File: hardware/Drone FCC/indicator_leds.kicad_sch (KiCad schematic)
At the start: 50 parts, among them Q1101 2N7002, Q1102 2N7002, Q1103 2N7002, Q1104 2N7002, Q1105 2N7002, Q1106 2N7002, Q1107 2N7002, Q1108 2N7002, SW1101 SW Proposito General, SW1102 SW Proposito General

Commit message: set values of resistors for LEDs
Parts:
- R1101, R1104, R1107, R1110, R1113, R1116, R1119, R1122: value R -> 100k
- R1102, R1105, R1108, R1111, R1114, R1117, R1120, R1123: value R -> 33k
- R1103, R1106, R1109, R1112, R1115, R1118, R1121, R1124: value R -> 220
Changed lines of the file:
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@@
   (junction (at 118.11 17.145) (diameter 0) (color 0 0 0 0)
   )
-  (junction (at 46.355 167.64) (diameter 0) (color 0 0 0 0)
-  )
   (junction (at 119.38 182.245) (diameter 0) (color 0 0 0 0)
   )
@@
     (stroke (width 0) (type default) (color 0 0 0 0))
   )
-  (wire (pts (xy 46.355 167.64) (xy 46.355 167.005))
-    (stroke (width 0) (type default) (color 0 0 0 0))
-  )
   (wire (pts (xy 118.11 29.845) (xy 118.11 32.385))
     (stroke (width 0) (type default) (color 0 0 0 0))
@@
     (stroke (width 0) (type default) (color 0 0 0 0))
   )
-  (wire (pts (xy 42.545 167.64) (xy 46.355 167.64))
-    (stroke (width 0) (type default) (color 0 0 0 0))
-  )
   (wire (pts (xy 40.005 167.64) (xy 42.545 167.64))
     (stroke (width 0) (type default) (color 0 0 0 0))
@@
     (stroke (width 0) (type default) (color 0 0 0 0))
   )
-  (wire (pts (xy 46.355 167.64) (xy 51.435 167.64))
+  (wire (pts (xy 42.545 167.64) (xy 51.435 167.64))
     (stroke (width 0) (type default) (color 0 0 0 0))
   )
@@
     (in_bom yes) (on_board yes) (fields_autoplaced)
     (property "Reference" "R1102" (id 0) (at 55.88 41.91 90))
-    (property "Value" "R" (id 1) (at 55.88 44.45 90))
+    (property "Value" "33k" (id 1) (at 55.88 44.45 90))
     (property "Footprint" "Resistor_SMD:R_0402_1005Metric_Pad0.72x0.64mm_HandSolder" (id 2) (at 55.88 49.403 90)
       (effects (font (size 1.27 1.27)) hide)
@@
   (symbol (lib_id "Device:R") (at 95.885 133.985 180) (unit 1)
     (in_bom yes) (on_board yes) (fields_autoplaced)
-    (property "Reference" "R1116" (id 0) (at 98.425 132.7149 0)
-      (effects (font (size 1.27 1.27)) (justify right))
-    )
-    (property "Value" "R" (id 1) (at 98.425 135.2549 0)
+    (property "Reference" "R1116" (id 0) (at 97.79 132.7149 0)
+      (effects (font (size 1.27 1.27)) (justify right))
+    )
+    (property "Value" "100k" (id 1) (at 97.79 135.2549 0)
       (effects (font (size 1.27 1.27)) (justify right))
     )
@@
   (symbol (lib_id "Device:R") (at 47.625 133.985 180) (unit 1)
     (in_bom yes) (on_board yes) (fields_autoplaced)
-    (property "Reference" "R1113" (id 0) (at 50.165 132.7149 0)
-      (effects (font (size 1.27 1.27)) (justify right))
-    )
-    (property "Value" "R" (id 1) (at 50.165 135.2549 0)
+    (property "Reference" "R1113" (id 0) (at 49.53 132.7149 0)
+      (effects (font (size 1.27 1.27)) (justify right))
+    )
+    (property "Value" "100k" (id 1) (at 49.53 135.2549 0)
       (effects (font (size 1.27 1.27)) (justify right))
     )
@@
       (effects (font (size 1.27 1.27)) (justify right))
     )
-    (property "Value" "R" (id 1) (at 175.26 135.2549 0)
+    (property "Value" "100k" (id 1) (at 175.26 135.2549 0)
       (effects (font (size 1.27 1.27)) (justify right))
     )
@@
   (symbol (lib_id "Device:R") (at 67.945 116.205 180) (unit 1)
     (in_bom yes) (on_board yes) (fields_autoplaced)
-    (property "Reference" "R1115" (id 0) (at 70.485 114.9349 0)
-      (effects (font (size 1.27 1.27)) (justify right))
-    )
-    (property "Value" "R" (id 1) (at 70.485 117.4749 0)
+    (property "Reference" "R1115" (id 0) (at 69.85 114.9349 0)
+      (effects (font (size 1.27 1.27)) (justify right))
+    )
+    (property "Value" "220" (id 1) (at 69.85 117.4749 0)
       (effects (font (size 1.27 1.27)) (justify right))
     )
@@
       (effects (font (size 1.27 1.27)) (justify right))
     )
-    (property "Value" "R" (id 1) (at 243.84 37.4649 0)
+    (property "Value" "220" (id 1) (at 243.84 37.4649 0)
       (effects (font (size 1.27 1.27)) (justify right))
     )
@@
       (effects (font (size 1.27 1.27)) (justify right))
     )
-    (property "Value" "R" (id 1) (at 223.52 55.2449 0)
+    (property "Value" "100k" (id 1) (at 223.52 55.2449 0)
       (effects (font (size 1.27 1.27)) (justify right))
     )
@@
       (effects (font (size 1.27 1.27)) (justify right))
     )
-    (property "Value" "R" (id 1) (at 120.65 37.4649 0)
+    (property "Value" "220" (id 1) (at 120.65 37.4649 0)
       (effects (font (size 1.27 1.27)) (justify right))
     )
@@
     (in_bom yes) (on_board yes) (fields_autoplaced)
     (property "Reference" "R1108" (id 0) (at 179.07 41.91 90))
-    (property "Value" "R" (id 1) (at 179.07 44.45 90))
+    (property "Value" "33k" (id 1) (at 179.07 44.45 90))
     (property "Footprint" "Resistor_SMD:R_0402_1005Metric_Pad0.72x0.64mm_HandSolder" (id 2) (at 179.07 49.403 90)
       (effects (font (size 1.27 1.27)) hide)
@@
     (in_bom yes) (on_board yes) (fields_autoplaced)
     (property "Reference" "R1114" (id 0) (at 53.975 121.92 90))
-    (property "Value" "R" (id 1) (at 53.975 124.46 90))
+    (property "Value" "33k" (id 1) (at 53.975 124.46 90))
     (property "Footprint" "Resistor_SMD:R_0402_1005Metric_Pad0.72x0.64mm_HandSolder" (id 2) (at 53.975 129.413 90)
       (effects (font (size 1.27 1.27)) hide)
@@
       (effects (font (size 1.27 1.27)) (justify right))
     )
-    (property "Value" "R" (id 1) (at 72.39 37.4649 0)
+    (property "Value" "220" (id 1) (at 72.39 37.4649 0)
       (effects (font (size 1.27 1.27)) (justify right))
     )
@@
       (effects (font (size 1.27 1.27)) (justify right))
     )
-    (property "Value" "R" (id 1) (at 52.07 55.2449 0)
+    (property "Value" "100k" (id 1) (at 52.07 55.2449 0)
       (effects (font (size 1.27 1.27)) (justify right))
     )
@@
       (effects (font (size 1.27 1.27)) (justify right))
     )
-    (property "Value" "R" (id 1) (at 223.52 135.2549 0)
+    (property "Value" "100k" (id 1) (at 223.52 135.2549 0)
       (effects (font (size 1.27 1.27)) (justify right))
     )
@@
     (in_bom yes) (on_board yes) (fields_autoplaced)
     (property "Reference" "R1123" (id 0) (at 227.33 121.92 90))
-    (property "Value" "R" (id 1) (at 227.33 124.46 90))
+    (property "Value" "33k" (id 1) (at 227.33 124.46 90))
     (property "Footprint" "Resistor_SMD:R_0402_1005Metric_Pad0.72x0.64mm_HandSolder" (id 2) (at 227.33 129.413 90)
       (effects (font (size 1.27 1.27)) hide)
@@
       (effects (font (size 1.27 1.27)) (justify right))
     )
-    (property "Value" "R" (id 1) (at 100.33 55.2449 0)
+    (property "Value" "100k" (id 1) (at 100.33 55.2449 0)
       (effects (font (size 1.27 1.27)) (justify right))
     )
@@
       (effects (font (size 1.27 1.27)) (justify right))
     )
-    (property "Value" "R" (id 1) (at 195.58 117.4749 0)
+    (property "Value" "220" (id 1) (at 195.58 117.4749 0)
       (effects (font (size 1.27 1.27)) (justify right))
     )
@@
       (effects (font (size 1.27 1.27)) (justify right))
     )
-    (property "Value" "R" (id 1) (at 175.26 55.2449 0)
+    (property "Value" "100k" (id 1) (at 175.26 55.2449 0)
       (effects (font (size 1.27 1.27)) (justify right))
     )
@@
     (in_bom yes) (on_board yes) (fields_autoplaced)
     (property "Reference" "R1120" (id 0) (at 179.07 121.92 90))
-    (property "Value" "R" (id 1) (at 179.07 124.46 90))
+    (property "Value" "33k" (id 1) (at 179.07 124.46 90))
     (property "Footprint" "Resistor_SMD:R_0402_1005Metric_Pad0.72x0.64mm_HandSolder" (id 2) (at 179.07 129.413 90)
       (effects (font (size 1.27 1.27)) hide)
@@
     (in_bom yes) (on_board yes) (fields_autoplaced)
     (property "Reference" "R1105" (id 0) (at 104.14 41.91 90))
-    (property "Value" "R" (id 1) (at 104.14 44.45 90))
+    (property "Value" "33k" (id 1) (at 104.14 44.45 90))
     (property "Footprint" "Resistor_SMD:R_0402_1005Metric_Pad0.72x0.64mm_HandSolder" (id 2) (at 104.14 49.403 90)
       (effects (font (size 1.27 1.27)) hide)
@@
       (effects (font (size 1.27 1.27)) (justify right))
     )
-    (property "Value" "R" (id 1) (at 243.84 117.4749 0)
+    (property "Value" "220" (id 1) (at 243.84 117.4749 0)
       (effects (font (size 1.27 1.27)) (justify right))
     )
@@
     (in_bom yes) (on_board yes) (fields_autoplaced)
     (property "Reference" "R1117" (id 0) (at 102.235 121.92 90))
-    (property "Value" "R" (id 1) (at 102.235 124.46 90))
+    (property "Value" "33k" (id 1) (at 102.235 124.46 90))
     (property "Footprint" "Resistor_SMD:R_0402_1005Metric_Pad0.72x0.64mm_HandSolder" (id 2) (at 102.235 129.413 90)
       (effects (font (size 1.27 1.27)) hide)
@@
       (effects (font (size 1.27 1.27)) (justify right))
     )
-    (property "Value" "R" (id 1) (at 195.58 37.4649 0)
+    (property "Value" "220" (id 1) (at 195.58 37.4649 0)
       (effects (font (size 1.27 1.27)) (justify right))
     )
@@
     (in_bom yes) (on_board yes) (fields_autoplaced)
     (property "Reference" "R1111" (id 0) (at 227.33 41.91 90))
-    (property "Value" "R" (id 1) (at 227.33 44.45 90))
+    (property "Value" "33k" (id 1) (at 227.33 44.45 90))
     (property "Footprint" "Resistor_SMD:R_0402_1005Metric_Pad0.72x0.64mm_HandSolder" (id 2) (at 227.33 49.403 90)
       (effects (font (size 1.27 1.27)) hide)
@@
   (symbol (lib_id "Device:R") (at 116.205 116.205 180) (unit 1)
     (in_bom yes) (on_board yes) (fields_autoplaced)
-    (property "Reference" "R1118" (id 0) (at 118.745 114.9349 0)
-      (effects (font (size 1.27 1.27)) (justify right))
-    )
-    (property "Value" "R" (id 1) (at 118.745 117.4749 0)
-      (effects (font (size 1.27 1.27)) (justify right))
-    )
+    (property "Reference" "R1118" (id 0) (at 118.11 114.9349 0)
+      (effects (font (size 1.27 1.27)) (justify right))
+    )
+    (property "Value" "220" (id 1) (at 118.11 117.4749 0)
+      (effects (font (size 1.27 1.27)) (justify right))
+    )

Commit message: moved some LEDs over the oppsoite layer of microSD footprint
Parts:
- R1103, R1106, R1109, R1112, R1115, R1118, R1121, R1124: footprint Resistor_SMD:R_0805_2012Metric_Pad1.20x1.40mm_HandSolder -> Resistor_SMD:R_0402_1005Metric_Pad0.72x0.64mm_HandSolder

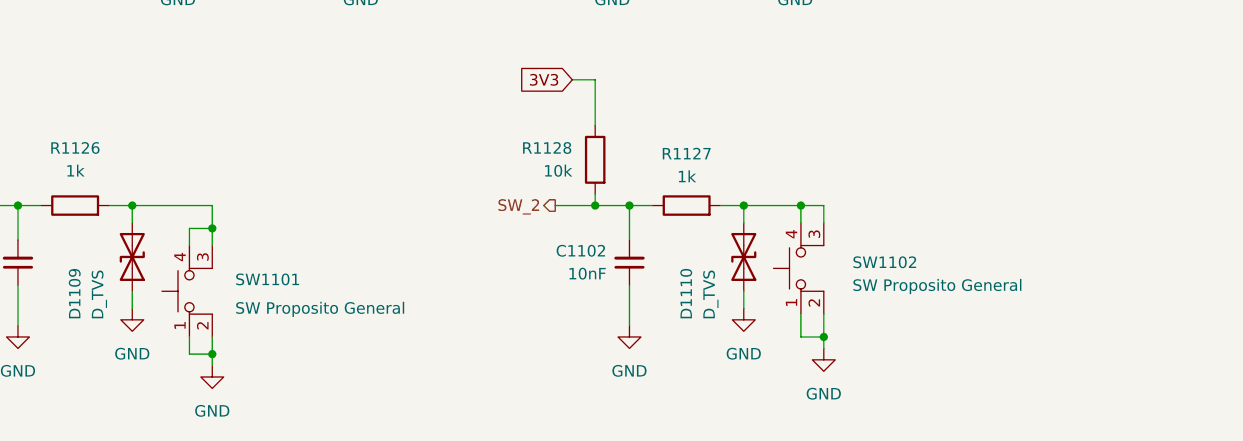
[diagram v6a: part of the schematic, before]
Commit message: changed sw with smaller sw
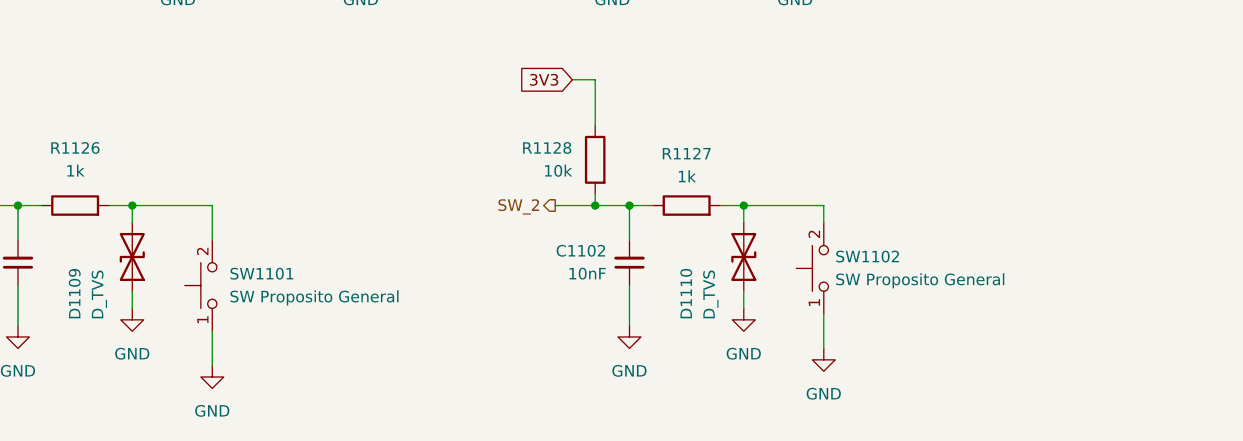
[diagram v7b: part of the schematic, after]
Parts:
- removed SW1101, SW1102: SW Proposito General, TL3305AF160QG:SW_TL3305AF160QG, symbol Switch:SW_MEC_5E
- added SW1101, SW1102: SW Proposito General, 434121043816:434121043816, symbol 434121043816:SW_SPST
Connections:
- net GND: now also SW1101.1 (A), SW1102.1 (A)
- net at D1110.2 (A2), R1127.2: now also SW1102.2 (B)
- net at D1109.2 (A2), R1126.2: now also SW1101.2 (B)
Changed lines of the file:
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@@
   (junction (at 118.11 17.145) (diameter 0) (color 0 0 0 0)
   )
-  (junction (at 119.38 182.245) (diameter 0) (color 0 0 0 0)
-  )
-  (junction (at 51.435 170.18) (diameter 0) (color 0 0 0 0)
-  )
   (junction (at 29.845 167.64) (diameter 0) (color 0 0 0 0)
   )
@@
   (junction (at 67.945 97.155) (diameter 0) (color 0 0 0 0)
   )
-  (junction (at 51.435 184.15) (diameter 0) (color 0 0 0 0)
-  )
   (junction (at 26.035 167.64) (diameter 0) (color 0 0 0 0)
   )
@@
   (junction (at 116.205 97.155) (diameter 0) (color 0 0 0 0)
   )
-  (junction (at 116.84 167.64) (diameter 0) (color 0 0 0 0)
-  )
   (junction (at 193.04 97.155) (diameter 0) (color 0 0 0 0)
   )
@@
     (stroke (width 0) (type default) (color 0 0 0 0))
   )
-  (wire (pts (xy 116.84 167.64) (xy 116.84 169.545))
+  (wire (pts (xy 51.435 167.64) (xy 51.435 171.45))
     (stroke (width 0) (type default) (color 0 0 0 0))
   )
@@
     (stroke (width 0) (type default) (color 0 0 0 0))
   )
-  (wire (pts (xy 51.435 184.15) (xy 51.435 185.42))
-    (stroke (width 0) (type default) (color 0 0 0 0))
-  )
   (wire (pts (xy 193.04 132.715) (xy 193.04 140.335))
     (stroke (width 0) (type default) (color 0 0 0 0))
@@
     (stroke (width 0) (type default) (color 0 0 0 0))
   )
-  (wire (pts (xy 116.84 167.64) (xy 119.38 167.64))
+  (wire (pts (xy 110.49 167.64) (xy 119.38 167.64))
     (stroke (width 0) (type default) (color 0 0 0 0))
   )
@@
     (stroke (width 0) (type default) (color 0 0 0 0))
   )
-  (wire (pts (xy 48.895 170.18) (xy 51.435 170.18))
-    (stroke (width 0) (type default) (color 0 0 0 0))
-  )
   (wire (pts (xy 89.535 167.64) (xy 93.98 167.64))
     (stroke (width 0) (type default) (color 0 0 0 0))
@@
     (stroke (width 0) (type default) (color 0 0 0 0))
   )
-  (wire (pts (xy 51.435 170.18) (xy 51.435 172.085))
-    (stroke (width 0) (type default) (color 0 0 0 0))
-  )
   (wire (pts (xy 57.785 127.635) (xy 60.325 127.635))
     (stroke (width 0) (type default) (color 0 0 0 0))
@@
     (stroke (width 0) (type default) (color 0 0 0 0))
   )
-  (wire (pts (xy 48.895 182.245) (xy 48.895 184.15))
-    (stroke (width 0) (type default) (color 0 0 0 0))
-  )
   (wire (pts (xy 40.005 167.64) (xy 42.545 167.64))
     (stroke (width 0) (type default) (color 0 0 0 0))
@@
     (stroke (width 0) (type default) (color 0 0 0 0))
   )
-  (wire (pts (xy 119.38 182.245) (xy 119.38 179.705))
+  (wire (pts (xy 119.38 179.705) (xy 119.38 183.515))
     (stroke (width 0) (type default) (color 0 0 0 0))
   )
@@
     (stroke (width 0) (type default) (color 0 0 0 0))
   )
-  (wire (pts (xy 48.895 172.085) (xy 48.895 170.18))
-    (stroke (width 0) (type default) (color 0 0 0 0))
-  )
   (wire (pts (xy 167.64 127.635) (xy 172.72 127.635))
     (stroke (width 0) (type default) (color 0 0 0 0))
@@
     (stroke (width 0) (type default) (color 0 0 0 0))
   )
-  (wire (pts (xy 116.84 179.705) (xy 116.84 182.245))
-    (stroke (width 0) (type default) (color 0 0 0 0))
-  )
   (wire (pts (xy 193.04 109.855) (xy 193.04 112.395))
     (stroke (width 0) (type default) (color 0 0 0 0))
@@
     (stroke (width 0) (type default) (color 0 0 0 0))
   )
-  (wire (pts (xy 119.38 182.245) (xy 119.38 183.515))
-    (stroke (width 0) (type default) (color 0 0 0 0))
-  )
   (wire (pts (xy 64.77 17.145) (xy 69.85 17.145))
     (stroke (width 0) (type default) (color 0 0 0 0))
   )
+  (wire (pts (xy 51.435 181.61) (xy 51.435 185.42))
+    (stroke (width 0) (type default) (color 0 0 0 0))
+  )
   (wire (pts (xy 172.72 127.635) (xy 172.72 130.175))
     (stroke (width 0) (type default) (color 0 0 0 0))
   )
-  (wire (pts (xy 48.895 184.15) (xy 51.435 184.15))
-    (stroke (width 0) (type default) (color 0 0 0 0))
-  )
   (wire (pts (xy 118.11 52.705) (xy 118.11 60.325))
     (stroke (width 0) (type default) (color 0 0 0 0))
@@
     (stroke (width 0) (type default) (color 0 0 0 0))
   )
-  (wire (pts (xy 110.49 167.64) (xy 116.84 167.64))
-    (stroke (width 0) (type default) (color 0 0 0 0))
-  )
   (wire (pts (xy 100.33 167.64) (xy 97.79 167.64))
     (stroke (width 0) (type default) (color 0 0 0 0))
   )
-  (wire (pts (xy 116.84 182.245) (xy 119.38 182.245))
-    (stroke (width 0) (type default) (color 0 0 0 0))
-  )
   (wire (pts (xy 116.205 109.855) (xy 116.205 112.395))
     (stroke (width 0) (type default) (color 0 0 0 0))
@@
     (stroke (width 0) (type default) (color 0 0 0 0))
   )
-  (wire (pts (xy 51.435 167.64) (xy 51.435 170.18))
-    (stroke (width 0) (type default) (color 0 0 0 0))
-  )
   (wire (pts (xy 110.49 167.64) (xy 110.49 169.545))
     (stroke (width 0) (type default) (color 0 0 0 0))
@@
   )
   (wire (pts (xy 50.165 127.635) (xy 47.625 127.635))
-    (stroke (width 0) (type default) (color 0 0 0 0))
-  )
-  (wire (pts (xy 51.435 182.245) (xy 51.435 184.15))
     (stroke (width 0) (type default) (color 0 0 0 0))
   )
@@
     (pin "2")
   )
-  (symbol (lib_id "Switch:SW_MEC_5E") (at 51.435 177.165 90) (unit 1)
-    (in_bom yes) (on_board yes)
-    (property "Reference" "SW1101" (id 0) (at 53.975 175.895 90)
-      (effects (font (size 1.27 1.27)) (justify right))
-    )
-    (property "Value" "SW Proposito General" (id 1) (at 53.975 179.07 90)
-      (effects (font (size 1.27 1.27)) (justify right))
-    )
-    (property "Footprint" "TL3305AF160QG:SW_TL3305AF160QG" (id 2) (at 43.815 177.165 0)
-      (effects (font (size 1.27 1.27)) hide)
-    )
-    (property "Datasheet" "http://www.apem.com/int/index.php?controller=attachment&id_attachment=1371" (id 3) (at 43.815 177.165 0)
-      (effects (font (size 1.27 1.27)) hide)
-    )
-    (pin "1")
-    (pin "2")
-    (pin "3")
-    (pin "4")
-  )
   (symbol (lib_id "Device:R") (at 220.98 53.975 180) (unit 1)
     (in_bom yes) (on_board yes) (fields_autoplaced)
@@
     (pin "2")
   )
+  (symbol (lib_id "434121043816:SW_SPST") (at 119.38 174.625 90) (unit 1)
+    (in_bom yes) (on_board yes)
+    (property "Reference" "SW1102" (id 0) (at 120.65 173.3549 90)
+      (effects (font (size 1.27 1.27)) (justify right))
+    )
+    (property "Value" "SW Proposito General" (id 1) (at 120.65 175.8949 90)
+      (effects (font (size 1.27 1.27)) (justify right))
+    )
+    (property "Footprint" "434121043816:434121043816" (id 2) (at 119.38 174.625 0)
+      (effects (font (size 1.27 1.27)) hide)
+    )
+    (property "Datasheet" "~" (id 3) (at 119.38 174.625 0)
+      (effects (font (size 1.27 1.27)) hide)
+    )
+    (pin "1")
+    (pin "2")
+  )
   (symbol (lib_id "Device:D_TVS") (at 42.545 173.355 270) (mirror x) (unit 1)
     (in_bom yes) (on_board yes)
@@
     (pin "1")
   )
+  (symbol (lib_id "434121043816:SW_SPST") (at 51.435 176.53 90) (unit 1)
+    (in_bom yes) (on_board yes) (fields_autoplaced)
+    (property "Reference" "SW1101" (id 0) (at 53.34 175.2599 90)
+      (effects (font (size 1.27 1.27)) (justify right))
+    )
+    (property "Value" "SW Proposito General" (id 1) (at 53.34 177.7999 90)
+      (effects (font (size 1.27 1.27)) (justify right))
+    )
+    (property "Footprint" "434121043816:434121043816" (id 2) (at 51.435 176.53 0)
+      (effects (font (size 1.27 1.27)) hide)
+    )
+    (property "Datasheet" "~" (id 3) (at 51.435 176.53 0)
+      (effects (font (size 1.27 1.27)) hide)
+    )
+    (pin "1")
+    (pin "2")
+  )
   (symbol (lib_id "Device:R") (at 97.79 53.975 180) (unit 1)
     (in_bom yes) (on_board yes) (fields_autoplaced)
@@
     (pin "1")
   )
-  (symbol (lib_id "Switch:SW_MEC_5E") (at 119.38 174.625 90) (unit 1)
-    (in_bom yes) (on_board yes)
-    (property "Reference" "SW1102" (id 0) (at 122.555 173.99 90)
-      (effects (font (size 1.27 1.27)) (justify right))
-    )
-    (property "Value" "SW Proposito General" (id 1) (at 122.555 176.53 90)
-      (effects (font (size 1.27 1.27)) (justify right))
-    )
-    (property "Footprint" "TL3305AF160QG:SW_TL3305AF160QG" (id 2) (at 111.76 174.625 0)
-      (effects (font (size 1.27 1.27)) hide)
-    )
-    (property "Datasheet" "http://www.apem.com/int/index.php?controller=attachment&id_attachment=1371" (id 3) (at 111.76 174.625 0)
-      (effects (font (size 1.27 1.27)) hide)
-    )
-    (pin "1")
-    (pin "2")
-    (pin "3")
-    (pin "4")
-  )
   (symbol (lib_id "Device:R") (at 227.33 47.625 90) (unit 1)
